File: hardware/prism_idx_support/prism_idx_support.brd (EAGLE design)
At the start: 27 x 15 mm, 8 parts

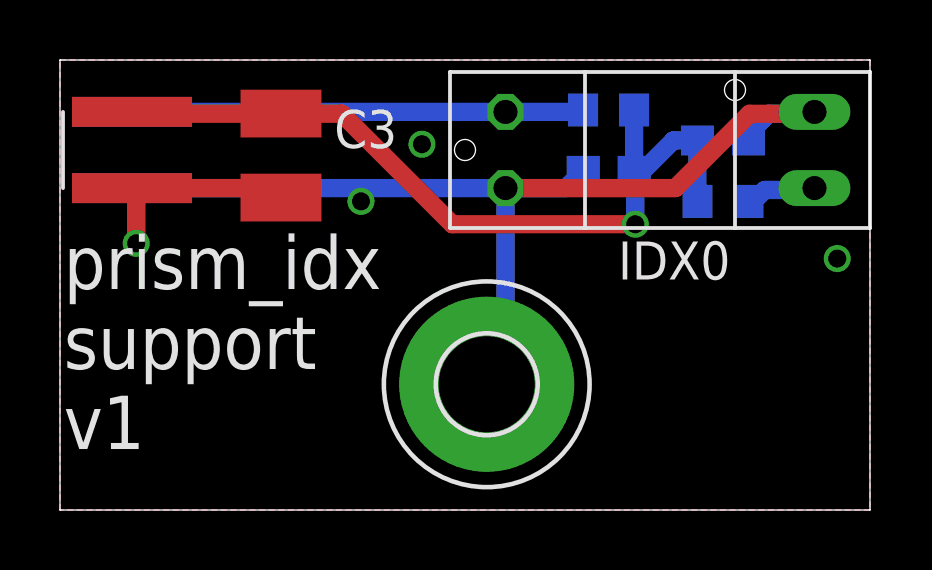
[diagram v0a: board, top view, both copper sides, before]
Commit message: resistor value modification after Damien review
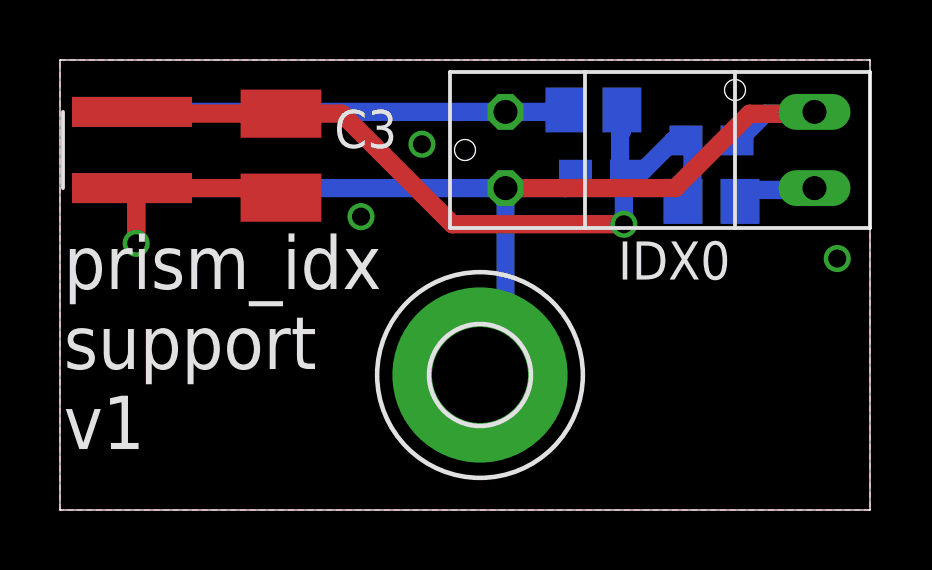
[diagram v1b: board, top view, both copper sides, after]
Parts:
- R1: value 270-F -> 100-E; device robotter_resistor:R0603 -> robotter_resistor:R0805
- R2: value 4K7-F -> 270-E; device robotter_resistor:R0603 -> robotter_resistor:R0805
- moved R2 0.51 mm to (17.8, 13.3)
- moved H1 0.38 mm to (14.0, 4.50)
- moved C1 0.38 mm to (21.7, 12.3)
- moved R1 0.38 mm to (21.7, 10.3)
- moved C2 0.28 mm to (18.0, 11.2)
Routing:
- net MIRROR_INDEX_1_3V3: track 15.1 -> 14.5 mm
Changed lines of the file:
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@@
 </autorouter>
 <elements>
-<element name="C1" library="robotter_capacitor" package="C0603" value="100nF 50V" x="22.098" y="12.319" smashed="yes" rot="MR180">
-<attribute name="RS" value=" 723-5534 " x="43.688" y="35.179" size="1.778" layer="28" rot="MR180" display="off"/>
-<attribute name="NAME" x="19.685" y="14.605" size="1.27" layer="26" rot="MR180"/>
-<attribute name="VALUE" x="21.463" y="14.224" size="1.27" layer="28" rot="MR180"/>
+<element name="C1" library="robotter_capacitor" package="C0603" value="100nF 50V" x="21.717" y="12.319" smashed="yes" rot="MR180">
+<attribute name="RS" value=" 723-5534 " x="43.307" y="35.179" size="1.778" layer="28" rot="MR180" display="off"/>
+<attribute name="NAME" x="19.304" y="14.605" size="1.27" layer="26" rot="MR180"/>
+<attribute name="VALUE" x="21.082" y="14.224" size="1.27" layer="28" rot="MR180"/>
 </element>
 <element name="IDX0" library="robotter_ic" package="GP1S58VJ000F" value="GP1S58VJ000F" x="20" y="12" smashed="yes">
@@
 <attribute name="VALUE" x="13.015" y="7.555" size="1.27" layer="27"/>
 </element>
-<element name="C2" library="robotter_capacitor" package="C0603" value="100nF 50V" x="18.288" y="11.303" smashed="yes" rot="MR0">
-<attribute name="RS" value=" 723-5534 " x="-14.732" y="-11.557" size="1.778" layer="28" rot="MR0" display="off"/>
-<attribute name="NAME" x="16.002" y="10.414" size="1.27" layer="26" rot="MR180"/>
-<attribute name="VALUE" x="18.923" y="9.398" size="1.27" layer="28" rot="MR0"/>
+<element name="C2" library="robotter_capacitor" package="C0603" value="100nF 50V" x="18.034" y="11.176" smashed="yes" rot="MR0">
+<attribute name="RS" value=" 723-5534 " x="-14.986" y="-11.684" size="1.778" layer="28" rot="MR0" display="off"/>
+<attribute name="NAME" x="15.748" y="10.287" size="1.27" layer="26" rot="MR180"/>
+<attribute name="VALUE" x="18.669" y="9.271" size="1.27" layer="28" rot="MR0"/>
 </element>
-<element name="R2" library="robotter_resistor" package="R0603" value="4K7-F" x="18.288" y="13.335" smashed="yes" rot="MR180">
-<attribute name="RS" value="740-8959" x="36.068" y="41.275" size="1.778" layer="28" rot="MR180" display="off"/>
-<attribute name="NAME" x="15.494" y="12.446" size="1.27" layer="26" rot="MR90"/>
-<attribute name="VALUE" x="17.653" y="15.24" size="1.27" layer="28" rot="MR180"/>
-</element>
-<element name="R1" library="robotter_resistor" package="R0603" value="270-F" x="22.098" y="10.287" smashed="yes" rot="MR0">
-<attribute name="RS" value=" 679-0071" x="-2.032" y="-17.653" size="1.778" layer="28" rot="MR0" display="off"/>
-<attribute name="NAME" x="22.987" y="8.001" size="1.27" layer="26" rot="MR0"/>
-<attribute name="VALUE" x="22.733" y="8.382" size="1.27" layer="28" rot="MR0"/>
-</element>
-<element name="H1" library="robotter_others" package="3,2-PAD" value="MOUNT-PAD-ROUND3.2" x="14.224" y="4.191"/>
+<element name="H1" library="robotter_others" package="3,2-PAD" value="MOUNT-PAD-ROUND3.2" x="14" y="4.5"/>
 <element name="IDX" library="robotter_others" package="PRISM_INDEX_EXTENSION_FEMALE" value="PRISM_INDEX_EXTENSION_FEMALE" x="2.4" y="12"/>
 <element name="C3" library="robotter_capacitor" package="C1210" value="10µF 25V" x="7.366" y="11.811" smashed="yes" rot="R270">
@@
 <attribute name="NAME" x="9.144" y="12.065" size="1.27" layer="25"/>
 <attribute name="VALUE" x="4.191" y="13.716" size="1.27" layer="27" rot="R270"/>
+</element>
+<element name="R2" library="robotter_resistor" package="R0805" value="270-E" x="17.78" y="13.335" rot="MR180">
+<attribute name="RS" value="740-9019" x="17.78" y="13.335" size="1.778" layer="28" rot="MR180" display="off"/>
+</element>
+<element name="R1" library="robotter_resistor" package="R0805" value="100-E" x="21.717" y="10.287" rot="MR0">
+<attribute name="RS" value="223-0297" x="21.717" y="10.287" size="1.778" layer="28" rot="MR0" display="off"/>
 </element>
 </elements>
@@
 <wire x1="22.987" y1="13.208" x2="25.088" y2="13.208" width="0.6096" layer="1"/>
 <wire x1="25.088" y1="13.208" x2="25.15" y2="13.27" width="0.6096" layer="1"/>
-<wire x1="22.948" y1="12.319" x2="22.948" y2="12.534" width="0.6096" layer="16"/>
-<wire x1="22.948" y1="12.534" x2="23.622" y2="13.208" width="0.6096" layer="16"/>
-<wire x1="23.622" y1="13.208" x2="25.527" y2="13.208" width="0.6096" layer="16"/>
+<wire x1="22.567" y1="12.319" x2="22.821" y2="12.534" width="0.6096" layer="16"/>
+<wire x1="22.821" y1="12.534" x2="23.495" y2="13.208" width="0.6096" layer="16"/>
+<wire x1="23.495" y1="13.208" x2="25.527" y2="13.208" width="0.6096" layer="16"/>
 <wire x1="25.527" y1="13.208" x2="25.654" y2="13.081" width="0.6096" layer="16"/>
 <wire x1="25.654" y1="13.081" x2="25.339" y2="13.081" width="0.6096" layer="16"/>
 <wire x1="25.339" y1="13.081" x2="25.15" y2="13.27" width="0.6096" layer="16"/>
-<wire x1="17.438" y1="11.303" x2="16.865" y2="10.73" width="0.6096" layer="16"/>
+<wire x1="17.184" y1="11.176" x2="16.865" y2="10.73" width="0.6096" layer="16"/>
 <wire x1="16.865" y1="10.73" x2="14.85" y2="10.73" width="0.6096" layer="16"/>
 <wire x1="2.4" y1="10.73" x2="2.54" y2="10.73" width="0.6096" layer="16"/>
@@
 <wire x1="14.85" y1="10.73" x2="2.4" y2="10.73" width="0.6096" layer="16"/>
 <contactref element="H1" pad="B3,2"/>
-<wire x1="14.224" y1="4.191" x2="14.85" y2="5.071" width="0.6096" layer="16"/>
+<wire x1="14" y1="4.5" x2="14.85" y2="5.071" width="0.6096" layer="16"/>
 <wire x1="14.85" y1="5.071" x2="14.85" y2="10.73" width="0.6096" layer="16"/>
 <polygon width="0.6096" layer="16">
@@
 </polygon>
 <via x="12.065" y="12.192" extent="1-16" drill="0.6" shape="octagon"/>
-<via x="10.033" y="10.287" extent="1-16" drill="0.6" shape="octagon"/>
+<via x="10.033" y="9.779" extent="1-16" drill="0.6" shape="octagon"/>
 <via x="25.908" y="8.382" extent="1-16" drill="0.6" shape="octagon"/>
 </signal>
 <signal name="+3V3">
 <contactref element="C2" pad="1"/>
-<contactref element="R2" pad="2"/>
 <contactref element="IDX" pad="2"/>
 <contactref element="C3" pad="1"/>
 <contactref element="C1" pad="1"/>
-<contactref element="R1" pad="2"/>
-<wire x1="19.138" y1="11.303" x2="19.431" y2="11.303" width="0.6096" layer="16"/>
+<wire x1="18.884" y1="11.176" x2="19.431" y2="11.303" width="0.6096" layer="16"/>
 <wire x1="19.431" y1="11.303" x2="20.447" y2="12.319" width="0.6096" layer="16"/>
-<wire x1="20.447" y1="12.319" x2="21.248" y2="12.319" width="0.6096" layer="16"/>
-<wire x1="19.138" y1="13.335" x2="19.138" y2="11.303" width="0.6096" layer="16"/>
-<wire x1="21.248" y1="10.287" x2="21.248" y2="12.319" width="0.6096" layer="16"/>
+<wire x1="20.447" y1="12.319" x2="20.867" y2="12.319" width="0.6096" layer="16"/>
 <wire x1="7.366" y1="13.211" x2="2.359" y2="13.211" width="0.6096" layer="1"/>
 <wire x1="2.359" y1="13.211" x2="2.4" y2="13.27" width="0.6096" layer="1"/>
 <wire x1="7.366" y1="13.211" x2="9.395" y2="13.211" width="0.6096" layer="1"/>
 <wire x1="9.395" y1="13.211" x2="13.081" y2="9.525" width="0.6096" layer="1"/>
-<wire x1="13.081" y1="9.525" x2="19.177" y2="9.525" width="0.6096" layer="1"/>
-<via x="19.177" y="9.525" extent="1-16" drill="0.6" shape="octagon"/>
-<wire x1="19.177" y1="9.525" x2="19.177" y2="11.264" width="0.6096" layer="16"/>
-<wire x1="19.177" y1="11.264" x2="19.138" y2="11.303" width="0.6096" layer="16"/>
+<wire x1="13.081" y1="9.525" x2="18.796" y2="9.525" width="0.6096" layer="1"/>
+<via x="18.796" y="9.525" extent="1-16" drill="0.6" shape="octagon"/>
+<wire x1="18.796" y1="9.525" x2="18.796" y2="11.01" width="0.6096" layer="16"/>
+<wire x1="18.796" y1="11.01" x2="18.884" y2="11.176" width="0.6096" layer="16"/>
+<contactref element="R2" pad="2"/>
+<contactref element="R1" pad="2"/>
+<wire x1="18.884" y1="11.176" x2="18.669" y2="11.303" width="0.6096" layer="16"/>
+<wire x1="18.669" y1="11.303" x2="18.669" y2="12.573" width="0.6096" layer="16"/>
+<wire x1="18.669" y1="12.573" x2="18.73" y2="12.634" width="0.6096" layer="16"/>
+<wire x1="18.73" y1="12.634" x2="18.73" y2="13.335" width="0.6096" layer="16"/>
+<wire x1="20.767" y1="10.287" x2="21.082" y2="10.602" width="0.6096" layer="16"/>
+<wire x1="21.082" y1="10.602" x2="21.082" y2="12.104" width="0.6096" layer="16"/>
+<wire x1="21.082" y1="12.104" x2="20.867" y2="12.319" width="0.6096" layer="16"/>
 </signal>
 <signal name="N$57">
 <contactref element="IDX0" pad="LED_A"/>
+<wire x1="25.088" y1="10.668" x2="25.15" y2="10.73" width="0.6096" layer="16"/>
 <contactref element="R1" pad="1"/>
-<wire x1="22.948" y1="10.287" x2="23.114" y2="10.287" width="0.6096" layer="16"/>
-<wire x1="23.114" y1="10.287" x2="23.495" y2="10.668" width="0.6096" layer="16"/>
-<wire x1="23.495" y1="10.668" x2="25.088" y2="10.668" width="0.6096" layer="16"/>
-<wire x1="25.088" y1="10.668" x2="25.15" y2="10.73" width="0.6096" layer="16"/>
+<wire x1="25.088" y1="10.668" x2="23.048" y2="10.668" width="0.6096" layer="16"/>
+<wire x1="23.048" y1="10.668" x2="22.667" y2="10.287" width="0.6096" layer="16"/>
 </signal>
 <signal name="MIRROR_INDEX_1_3V3">
 <contactref element="IDX0" pad="TRANSISTOR_C"/>
+<contactref element="IDX" pad="4"/>
+<wire x1="2.4" y1="13.27" x2="14.85" y2="13.27" width="0.6096" layer="16"/>
 <contactref element="R2" pad="1"/>
-<contactref element="IDX" pad="4"/>
-<wire x1="17.438" y1="13.335" x2="17.373" y2="13.27" width="0.6096" layer="16"/>
-<wire x1="17.373" y1="13.27" x2="14.85" y2="13.27" width="0.6096" layer="16"/>
-<wire x1="2.4" y1="13.27" x2="14.85" y2="13.27" width="0.6096" layer="16"/>
+<wire x1="14.85" y1="13.27" x2="16.765" y2="13.27" width="0.6096" layer="16"/>
+<wire x1="16.765" y1="13.27" x2="16.83" y2="13.335" width="0.6096" layer="16"/>
 </signal>
 </signals>
